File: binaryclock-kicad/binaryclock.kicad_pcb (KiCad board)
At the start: 2 copper layers, 100 x 80 mm, 19 parts, among them J1 Conn_01x03_Pin, J2 AVR-ISP-6, SW1 SW_Push, SW2 SW_Push, SW3 SW_Push, U1 ATmega48-20P, Y1 Crystal

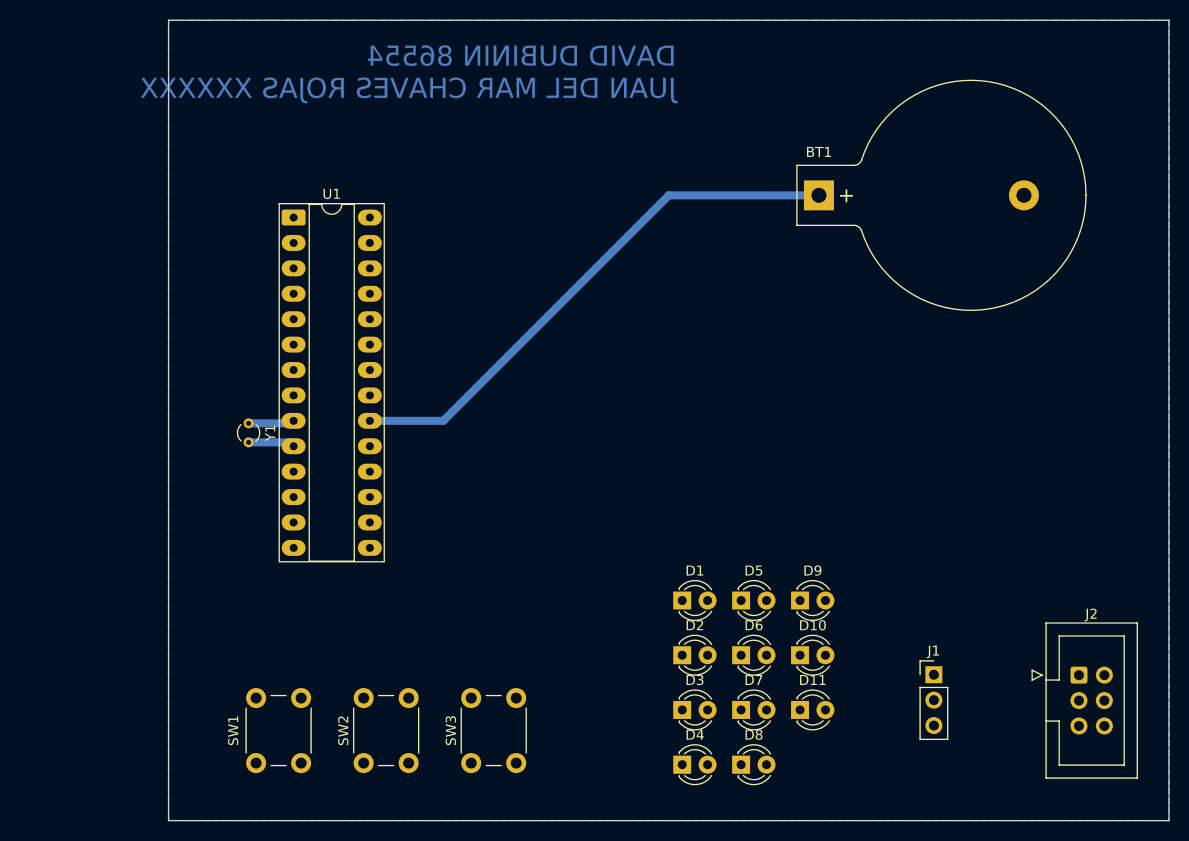
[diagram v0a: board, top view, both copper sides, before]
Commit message: passed drc
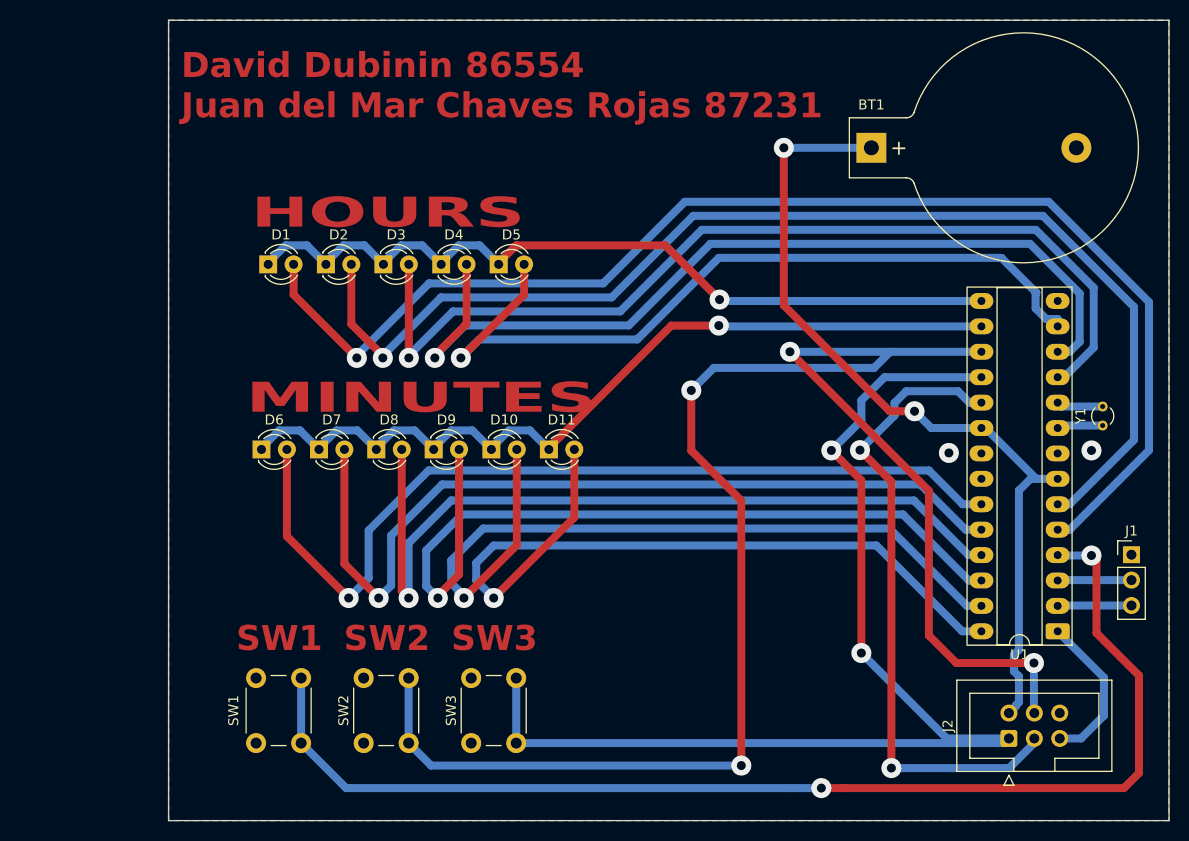
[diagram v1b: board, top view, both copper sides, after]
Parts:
- moved U1 86.9 mm to (143.9, 101.1), turned to 180 degrees
- moved Y1 85.4 mm to (148.4, 80.5), turned to 90 degrees
- moved D2 65.0 mm to (70.7, 64.4)
- moved D1 64.9 mm to (65.0, 64.4)
- moved D5 53.8 mm to (88.0, 64.4)
- moved D3 53.5 mm to (76.5, 64.4)
- moved D4 53.0 mm to (82.2, 64.4)
- moved D6 44.7 mm to (64.3, 82.9)
- moved D7 41.7 mm to (70.0, 82.9)
- moved D8 40.2 mm to (75.8, 82.9)
- moved D9 40.1 mm to (81.5, 82.9)
- moved D10 29.2 mm to (87.3, 82.9)
- moved D11 28.1 mm to (93.0, 82.9)
- moved J1 23.1 mm to (151.2, 93.4)
- moved J2 9.44 mm to (139.0, 111.8), turned to 90 degrees
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- renumbered D7 to D1, D5 to D10, D6 to D11, D8 to D2, D9 to D3, D10 to D4, D11 to D5, D1 to D6, D2 to D7, D3 to D8, D4 to D9
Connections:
- D1 pad 1: /OC1B -> /OC1A
- D10 pad 1: /OC1A -> /OC1B
- D11 pad 1: /OC1A -> /OC1B
- D2 pad 1: /OC1B -> /OC1A
- D3 pad 1: /OC1B -> /OC1A
- D4 pad 1: /OC1B -> /OC1A
- D5 pad 1: /OC1B -> /OC1A
- D6 pad 1: /OC1A -> /OC1B
- D7 pad 1: /OC1A -> /OC1B
- D8 pad 1: /OC1A -> /OC1B
- D9 pad 1: /OC1A -> /OC1B
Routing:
- net /MOSI/PCINT3: track 0.00 -> 171.9 mm, vias 0 -> 4
- net /PD3: track 0.00 -> 129.1 mm, vias 0 -> 1
- net /INT0: track 0.00 -> 119.9 mm, vias 0 -> 2
- net /PD4: track 0.00 -> 119.1 mm, vias 0 -> 1
- net /MISO/PCINT4: track 0.00 -> 114.9 mm, vias 0 -> 2
- net /PD5: track 0.00 -> 96.5 mm, vias 0 -> 1
- net /PC0: track 0.00 -> 90.3 mm, vias 0 -> 1
- net /PD6: track 0.00 -> 89.5 mm, vias 0 -> 1
- net /PC1: track 0.00 -> 86.0 mm, vias 0 -> 1
- net /OC1B: track 0.00 -> 85.5 mm, vias 0 -> 1
- net /PC2: track 0.00 -> 82.2 mm, vias 0 -> 1
- net /OC1A: track 0.00 -> 81.3 mm, vias 0 -> 1
- net /PC3: track 0.00 -> 80.7 mm, vias 0 -> 1
- net /PD7: track 0.00 -> 80.1 mm, vias 0 -> 1
- net /PC4: track 0.00 -> 78.8 mm, vias 0 -> 1
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- added copper zone on F.Cu, net -BATT
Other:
- board text added: "David Dubinin 86554 Juan del Mar Chaves Rojas 87231"
- board text added: "HOURS"
- board text added: "MINUTES"
- board text added: "SW1"
- board text added: "SW2"
- board text added: "SW3"
- board text removed: "DAVID DUBININ 86554 JUAN DEL MAR CHAVES ROJAS XXXXXX"
